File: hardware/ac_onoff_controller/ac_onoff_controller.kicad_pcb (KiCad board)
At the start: 2 copper layers, 100 x 52.5 mm, 40 parts, among them J1 Conn_02x04_Odd_Even, J2 Conn_01x02, M1 Motor_Servo, M2 Motor_Servo, Q1 2SK4017, Q2 2SK4017, Q3 2SC1815, Q6 2SK4017, SW1 SW_SPST, SW2 SW_Push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

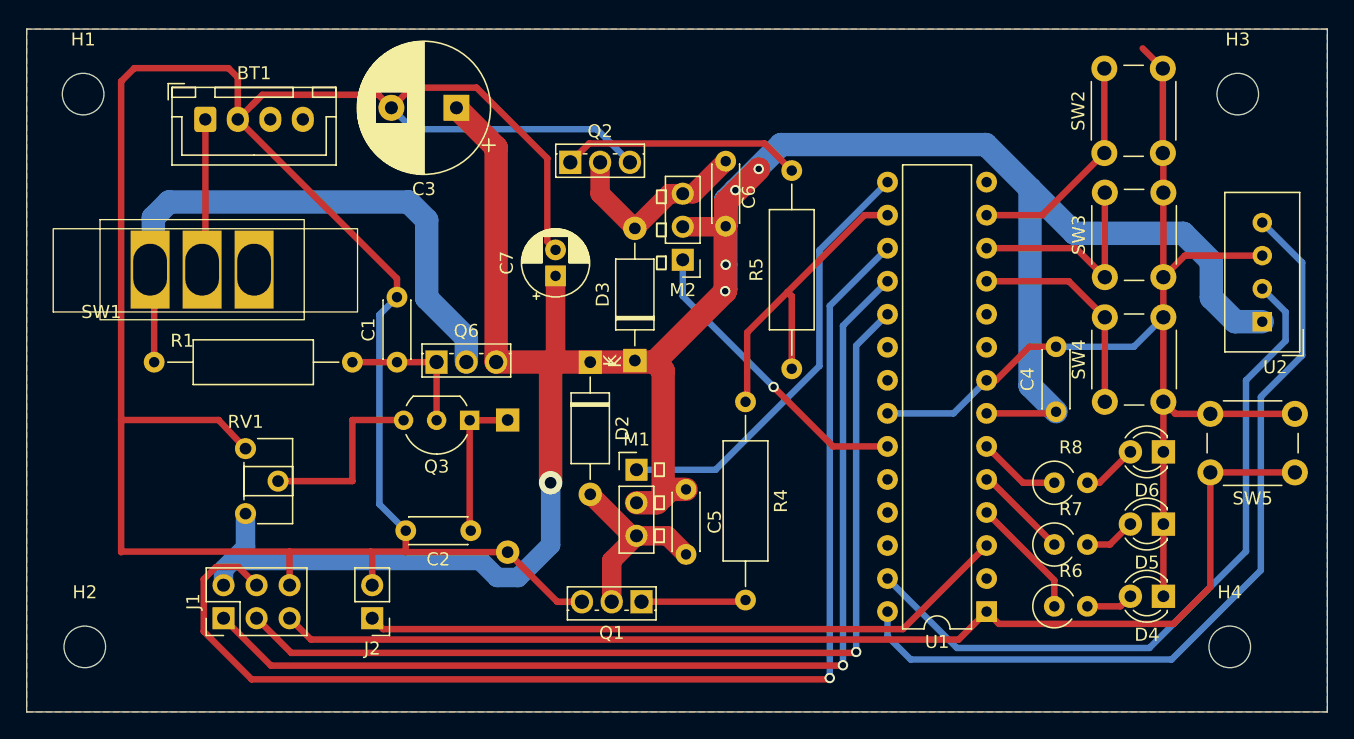
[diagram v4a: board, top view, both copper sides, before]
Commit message: add vias
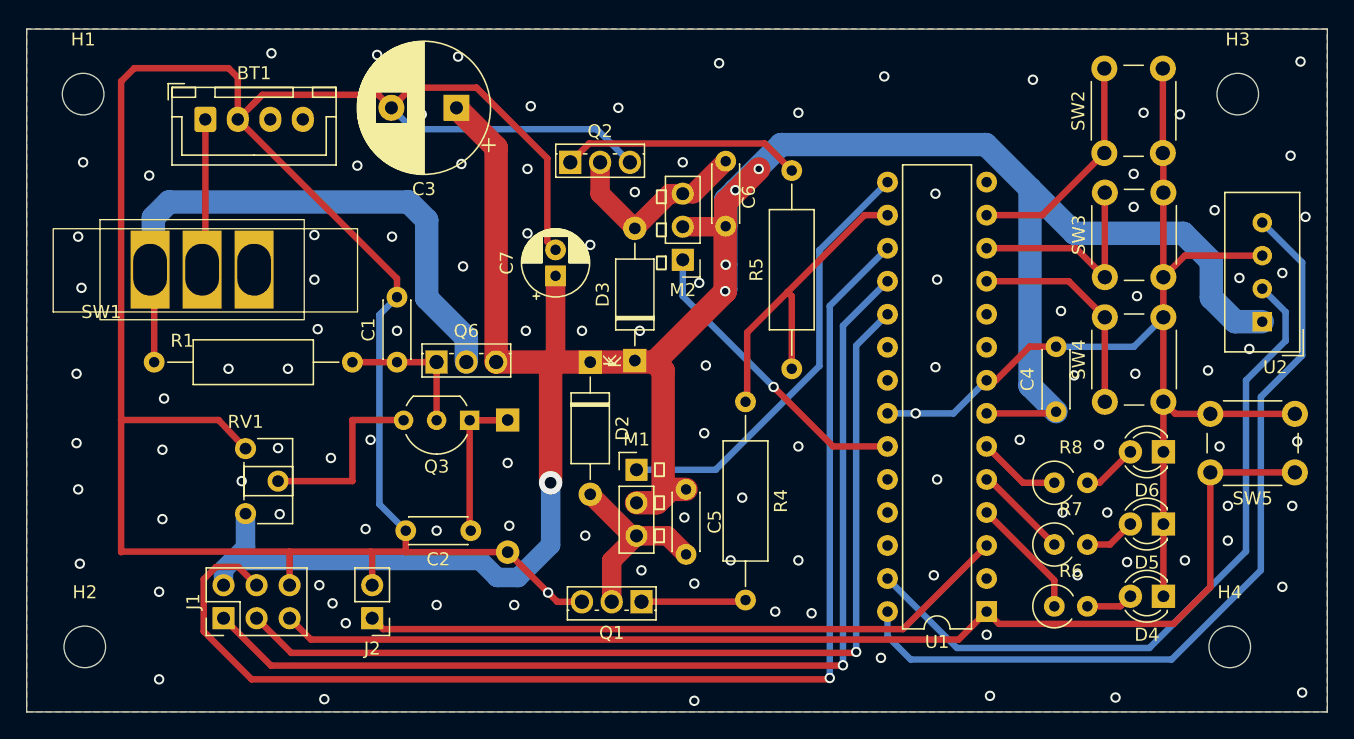
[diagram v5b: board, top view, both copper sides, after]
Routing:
- net GND: track 283.4 -> 281.2 mm, vias 0 -> 111
